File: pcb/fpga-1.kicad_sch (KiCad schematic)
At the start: 2 parts

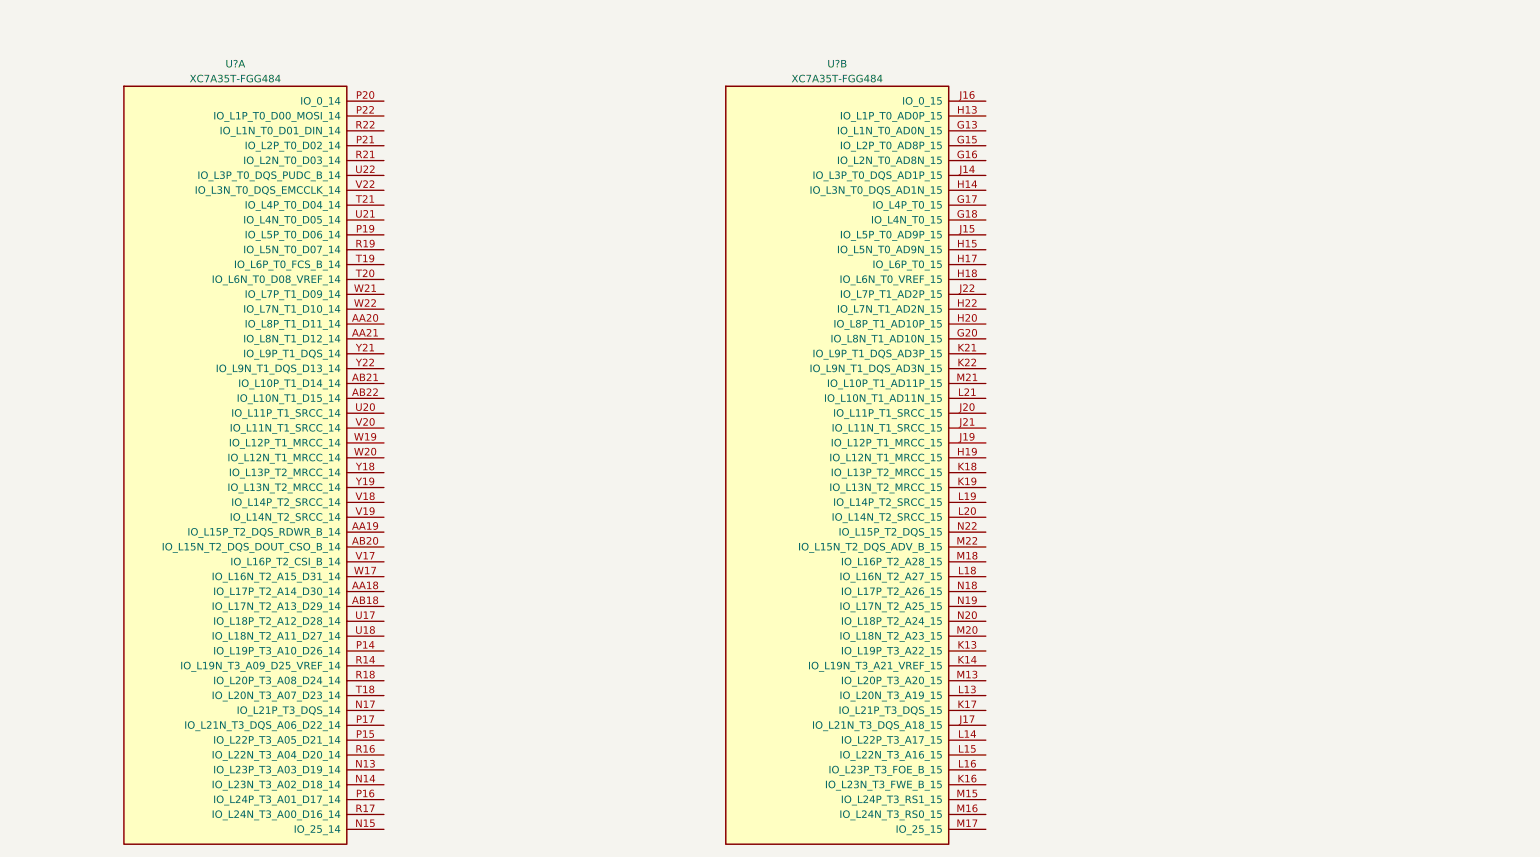
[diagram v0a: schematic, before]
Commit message: add sensors, hierarchical changes
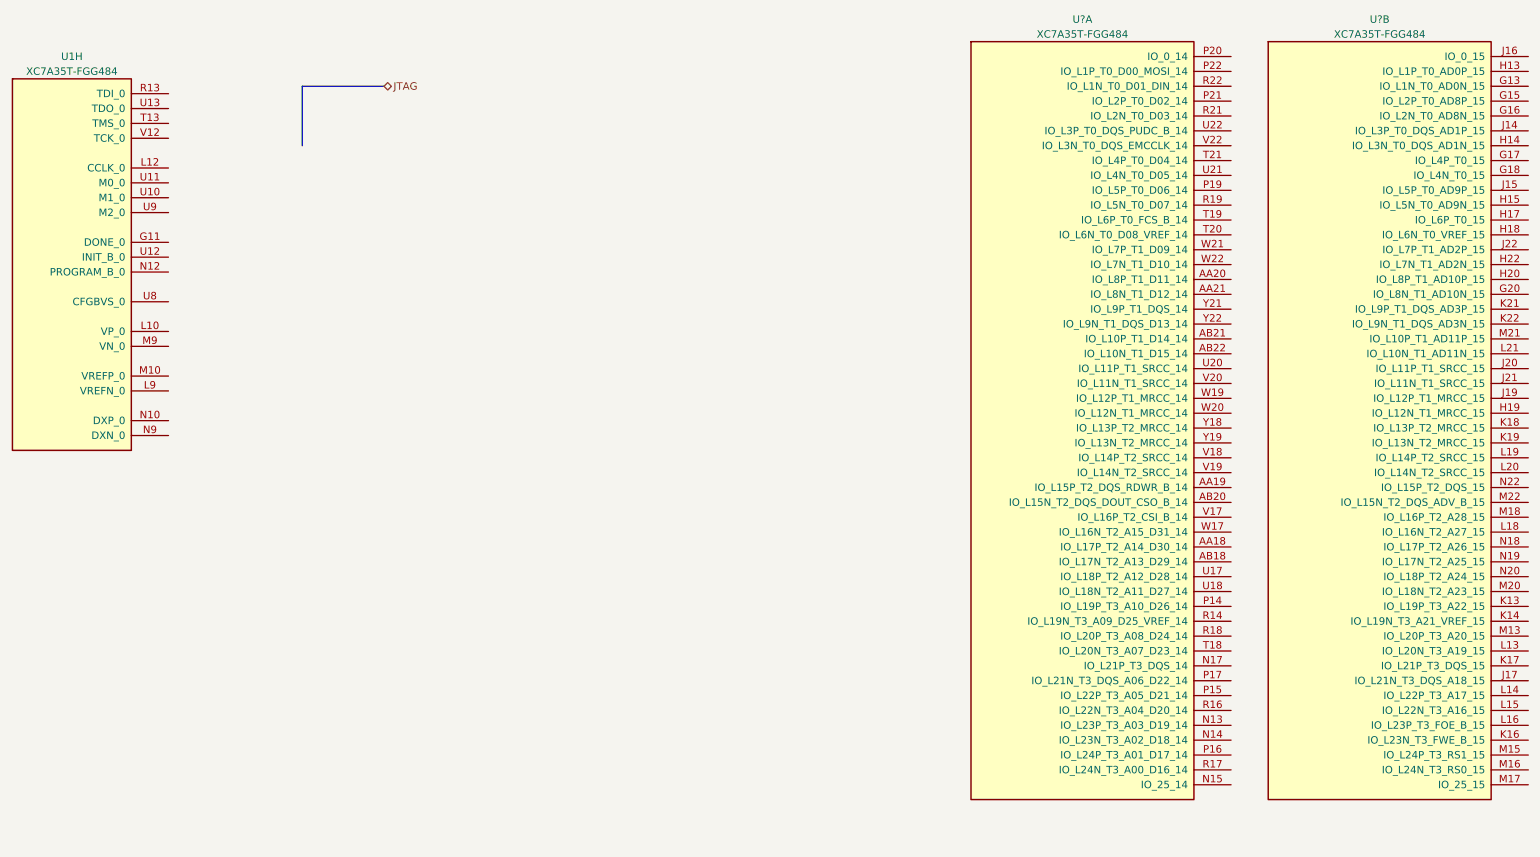
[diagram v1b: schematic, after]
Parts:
- added U1: XC7A35T-FGG484, Package_BGA:Xilinx_FGG484, symbol FPGA_Xilinx_Artix7:XC7A35T-FGG484
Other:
- moved on the sheet: U?A, U?B

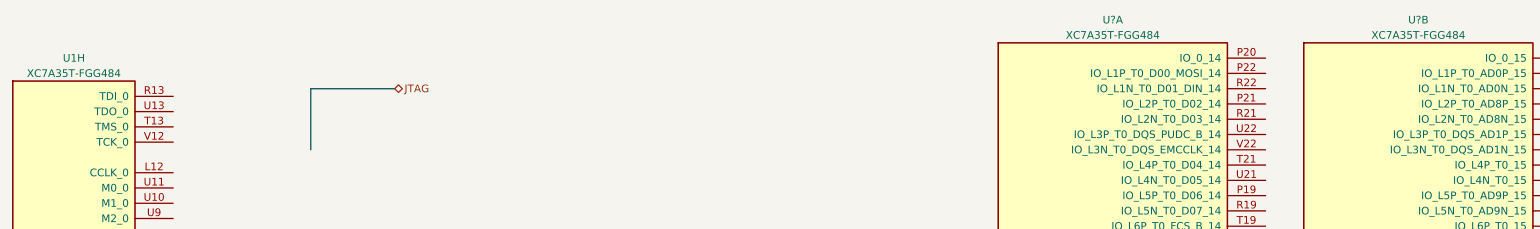
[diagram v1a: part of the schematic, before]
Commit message: addl. updates to power hierarchy
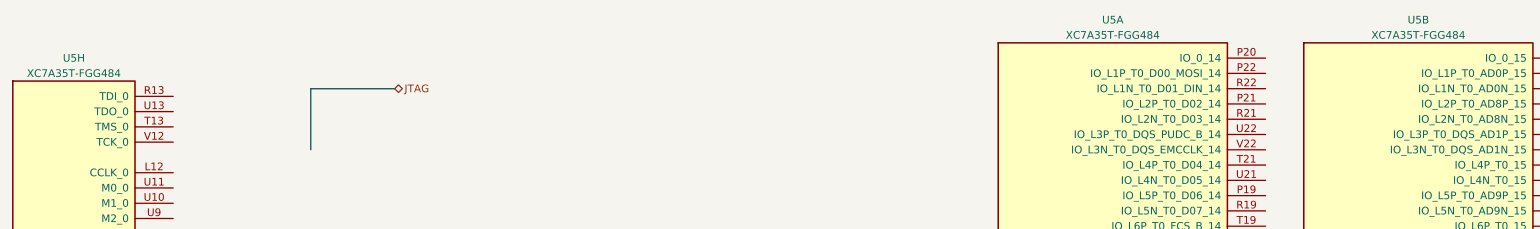
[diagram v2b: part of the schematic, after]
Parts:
- gave numbers to parts that had none: 1
- renumbered U1 to U5
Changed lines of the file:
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@@
 		(dnp no)
 		(fields_autoplaced yes)
-		(property "Reference" "U?"
+		(property "Reference" "U5"
 			(at 255.27 17.78 0)
 			(effects
@@
 			(project "RPi-HwAB-1"
 				(path "/e63e39d7-6ac0-4ffd-8aa3-1841a4541b55/74df7e7f-18cd-4565-8339-2ea0b43d6ca3"
-					(reference "U?")
+					(reference "U5")
 					(unit 2)
 				)
@@
 		(dnp no)
 		(fields_autoplaced yes)
-		(property "Reference" "U?"
+		(property "Reference" "U5"
 			(at 204.47 17.78 0)
 			(effects
@@
 			(project "RPi-HwAB-1"
 				(path "/e63e39d7-6ac0-4ffd-8aa3-1841a4541b55/74df7e7f-18cd-4565-8339-2ea0b43d6ca3"
-					(reference "U?")
+					(reference "U5")
 					(unit 1)
 				)
@@
 		(dnp no)
 		(fields_autoplaced yes)
-		(property "Reference" "U1"
+		(property "Reference" "U5"
 			(at 31.75 24.13 0)
 			(effects
@@
 			(project "RPi-HwAB-1"
 				(path "/e63e39d7-6ac0-4ffd-8aa3-1841a4541b55/74df7e7f-18cd-4565-8339-2ea0b43d6ca3"
-					(reference "U1")
+					(reference "U5")
 					(unit 8)
 				)

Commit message: added power sequencing through raspi gpio
additionally defined sensors
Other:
- company: (none) -> Andre S Winkel
- title: (none) -> RPi HwAB HAT+
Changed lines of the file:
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@@
 	(generator_version "9.0")
 	(paper "A4")
+	(title_block
+		(title "RPi HwAB HAT+")
+		(date "2025-08-23")
+		(rev "01")
+		(company "Andre S Winkel")
+	)
 	(bus
 		(pts

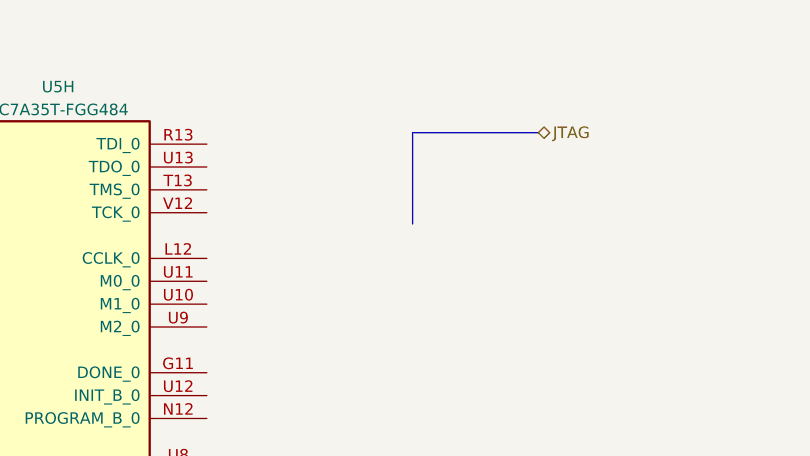
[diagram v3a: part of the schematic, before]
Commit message: added power supply simulations
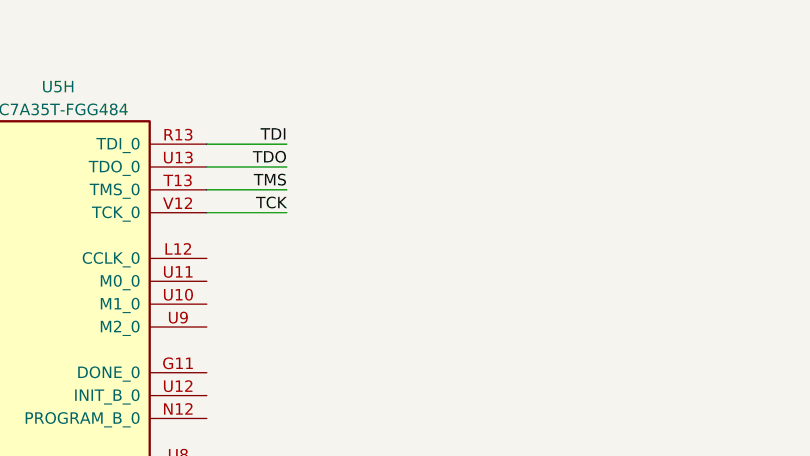
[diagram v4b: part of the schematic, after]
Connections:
- net TDI: now reaches U5.R13 (TDI_0)
- net TMS: now reaches U5.T13 (TMS_0)
- net TDO: now reaches U5.U13 (TDO_0)
- net TCK: now reaches U5.V12 (TCK_0)
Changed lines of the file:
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@@
 		(company "Andre S Winkel")
 	)
-	(bus
+	(wire
 		(pts
-			(xy 71.12 29.21) (xy 71.12 39.37)
+			(xy 48.26 30.48) (xy 57.15 30.48)
 		)
 		(stroke
@@
 		)
 	)
-	(bus
+	(wire
 		(pts
-			(xy 85.09 29.21) (xy 71.12 29.21)
+			(xy 48.26 33.02) (xy 57.15 33.02)
 		)
 		(stroke
@@
 		)
 	)
-	(hierarchical_label "JTAG"
-		(shape bidirectional)
-		(at 85.09 29.21 0)
+	(wire
+		(pts
+			(xy 48.26 35.56) (xy 57.15 35.56)
+		)
+		(stroke
+			(width 0)
+			(type default)
+		)
+	)
+	(wire
+		(pts
+			(xy 48.26 38.1) (xy 57.15 38.1)
+		)
+		(stroke
+			(width 0)
+			(type default)
+		)
+	)
+	(label "TDO"
+		(at 57.15 33.02 180)
 		(effects
 			(font
 				(size 1.27 1.27)
 			)
-			(justify left)
+			(justify right bottom)
 		)
 	)
+	(label "TCK"
+		(at 57.15 38.1 180)
+		(effects
+			(font
+				(size 1.27 1.27)
+			)
+			(justify right bottom)
+		)
+	)
+	(label "TMS"
+		(at 57.15 35.56 180)
+		(effects
+			(font
+				(size 1.27 1.27)
+			)
+			(justify right bottom)
+		)
+	)
+	(label "TDI"
+		(at 57.15 30.48 180)
+		(effects
+			(font
+				(size 1.27 1.27)
+			)
+			(justify right bottom)
+		)
+	)

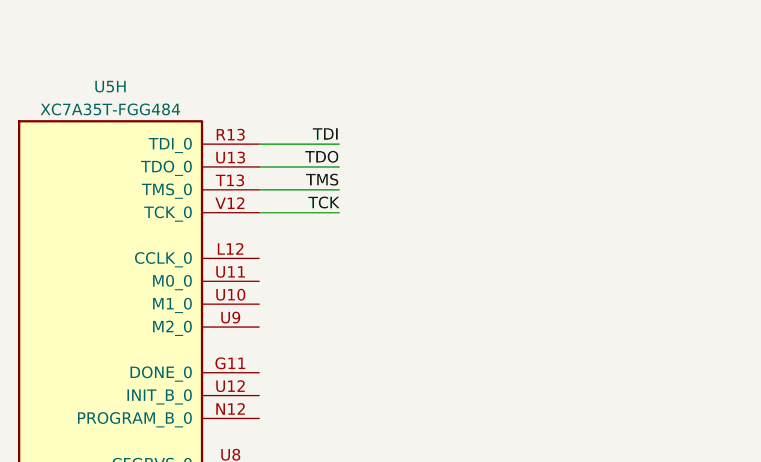
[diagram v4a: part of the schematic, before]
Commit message: connected jtag-fpga, tc2030
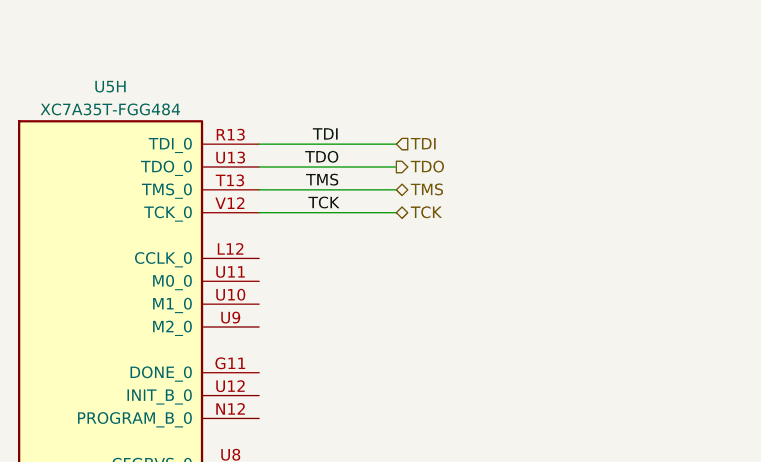
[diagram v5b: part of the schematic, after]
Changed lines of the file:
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@@
 	(wire
 		(pts
-			(xy 48.26 30.48) (xy 57.15 30.48)
+			(xy 48.26 30.48) (xy 63.5 30.48)
 		)
 		(stroke
@@
 	(wire
 		(pts
-			(xy 48.26 33.02) (xy 57.15 33.02)
+			(xy 48.26 33.02) (xy 63.5 33.02)
 		)
 		(stroke
@@
 	(wire
 		(pts
-			(xy 48.26 35.56) (xy 57.15 35.56)
+			(xy 48.26 35.56) (xy 63.5 35.56)
 		)
 		(stroke
@@
 	(wire
 		(pts
-			(xy 48.26 38.1) (xy 57.15 38.1)
+			(xy 48.26 38.1) (xy 63.5 38.1)
 		)
 		(stroke
@@
 		)
 	)
+	(hierarchical_label "TDI"
+		(shape input)
+		(at 63.5 30.48 0)
+		(effects
+			(font
+				(size 1.27 1.27)
+			)
+			(justify left)
+		)
+	)
+	(hierarchical_label "TDO"
+		(shape output)
+		(at 63.5 33.02 0)
+		(effects
+			(font
+				(size 1.27 1.27)
+			)
+			(justify left)
+		)
+	)
+	(hierarchical_label "TCK"
+		(shape bidirectional)
+		(at 63.5 38.1 0)
+		(effects
+			(font
+				(size 1.27 1.27)
+			)
+			(justify left)
+		)
+	)
+	(hierarchical_label "TMS"
+		(shape bidirectional)
+		(at 63.5 35.56 0)
+		(effects
+			(font
+				(size 1.27 1.27)
+			)
+			(justify left)
+		)
+	)

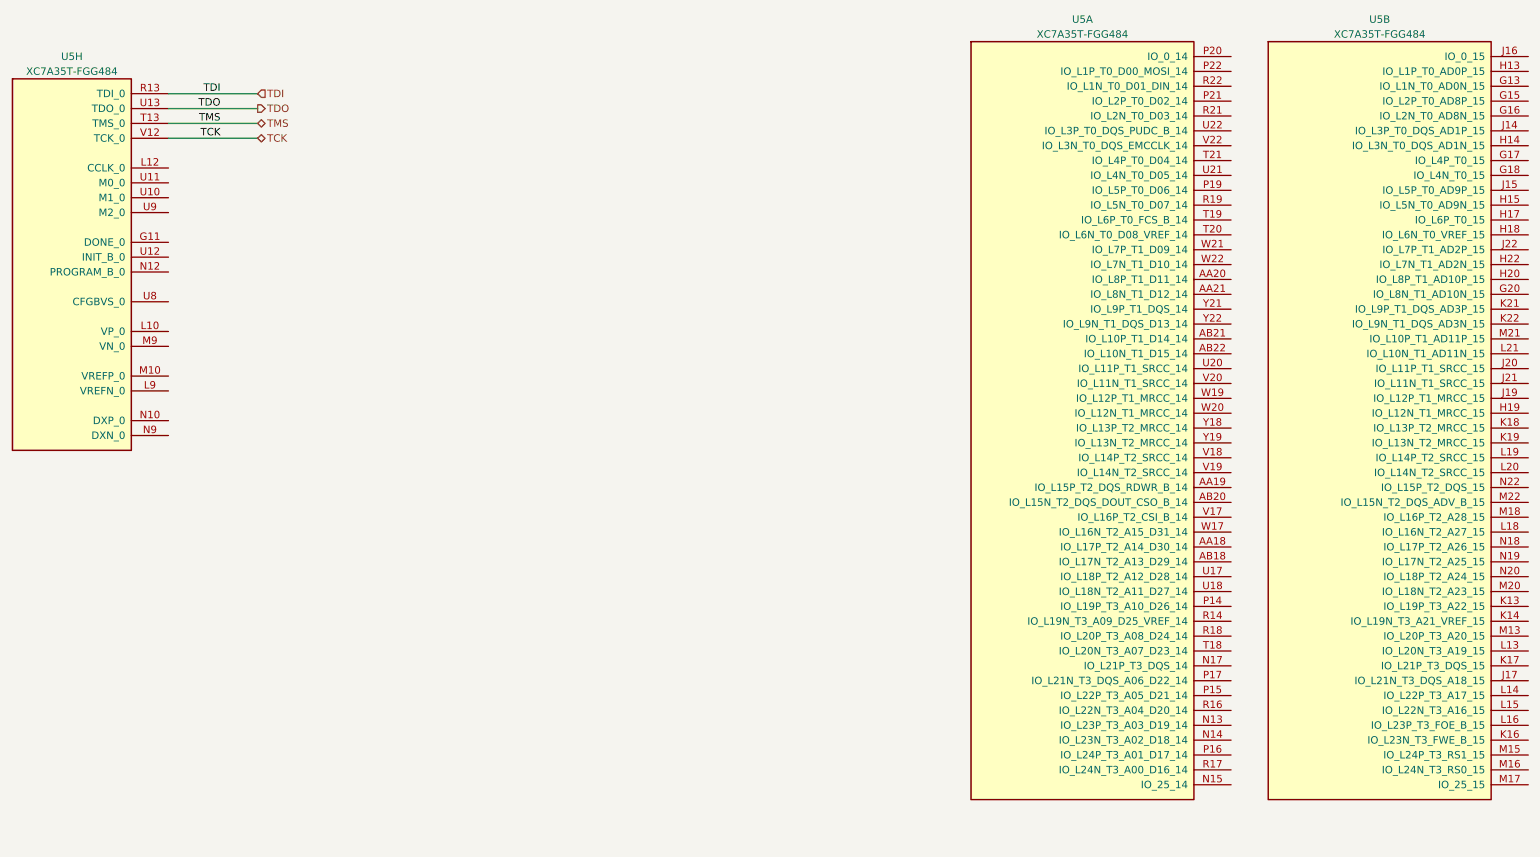
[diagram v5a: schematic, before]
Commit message: reorg hierarchical, define buses
added bus definitions, aliasing, reorganized sub-sheets for hierarchical interpretation, grouped fpga. pending dram and mram addition
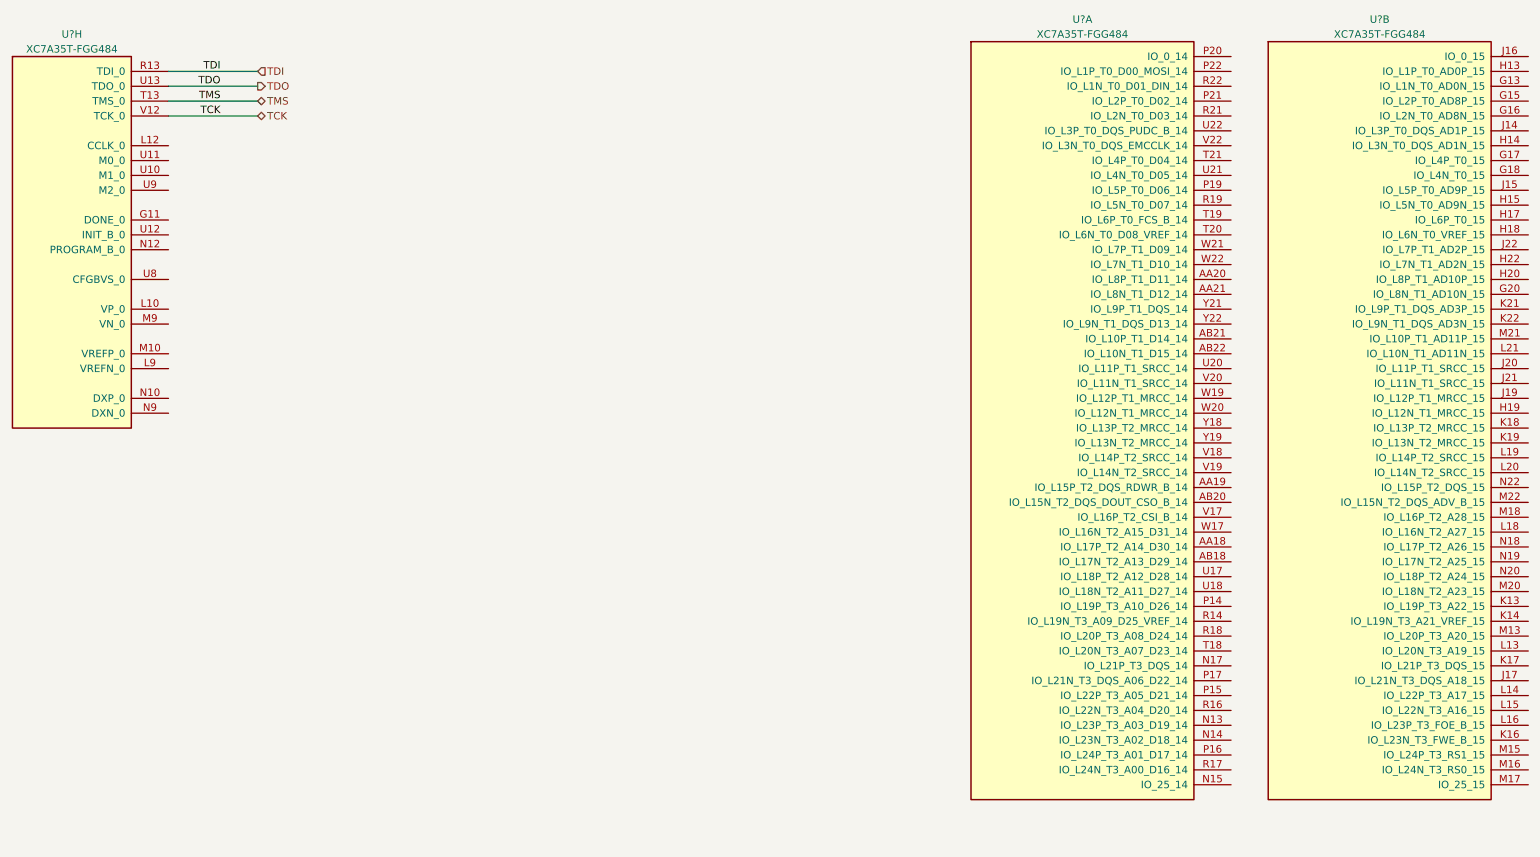
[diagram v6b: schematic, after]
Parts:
- renumbered U5 to U?
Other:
- moved on the sheet: U?H
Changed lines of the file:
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@@
 	(wire
 		(pts
-			(xy 48.26 30.48) (xy 63.5 30.48)
+			(xy 48.26 26.67) (xy 63.5 26.67)
 		)
 		(stroke
@@
 	(wire
 		(pts
-			(xy 48.26 33.02) (xy 63.5 33.02)
+			(xy 48.26 29.21) (xy 63.5 29.21)
 		)
 		(stroke
@@
 	(wire
 		(pts
-			(xy 48.26 35.56) (xy 63.5 35.56)
+			(xy 48.26 31.75) (xy 63.5 31.75)
 		)
 		(stroke
@@
 	(wire
 		(pts
-			(xy 48.26 38.1) (xy 63.5 38.1)
+			(xy 48.26 34.29) (xy 63.5 34.29)
 		)
 		(stroke
@@
 	)
 	(label "TDO"
-		(at 57.15 33.02 180)
+		(at 57.15 29.21 180)
 		(effects
 			(font
@@
 	)
 	(label "TCK"
-		(at 57.15 38.1 180)
+		(at 57.15 34.29 180)
 		(effects
 			(font
@@
 	)
 	(label "TMS"
-		(at 57.15 35.56 180)
+		(at 57.15 31.75 180)
 		(effects
 			(font
@@
 	)
 	(label "TDI"
-		(at 57.15 30.48 180)
+		(at 57.15 26.67 180)
 		(effects
 			(font
@@
 	(hierarchical_label "TDI"
 		(shape input)
-		(at 63.5 30.48 0)
+		(at 63.5 26.67 0)
 		(effects
 			(font
@@
 	(hierarchical_label "TDO"
 		(shape output)
-		(at 63.5 33.02 0)
+		(at 63.5 29.21 0)
 		(effects
 			(font
@@
 	(hierarchical_label "TCK"
 		(shape bidirectional)
-		(at 63.5 38.1 0)
+		(at 63.5 34.29 0)
 		(effects
 			(font
@@
 	(hierarchical_label "TMS"
 		(shape bidirectional)
-		(at 63.5 35.56 0)
+		(at 63.5 31.75 0)
 		(effects
 			(font
@@
 		(dnp no)
 		(fields_autoplaced yes)
-		(property "Reference" "U5"
+		(property "Reference" "U?"
 			(at 255.27 17.78 0)
 			(effects
@@
 		(instances
 			(project "RPi-HwAB-1"
-				(path "/e63e39d7-6ac0-4ffd-8aa3-1841a4541b55/74df7e7f-18cd-4565-8339-2ea0b43d6ca3"
-					(reference "U5")
+				(path "/e63e39d7-6ac0-4ffd-8aa3-1841a4541b55/59d21473-a004-4514-8090-fd93db818925/350bfe7d-9948-4ca7-a542-a75eb385def4"
+					(reference "U?")
 					(unit 2)
 				)
@@
 		(dnp no)
 		(fields_autoplaced yes)
-		(property "Reference" "U5"
+		(property "Reference" "U?"
 			(at 204.47 17.78 0)
 			(effects
@@
 		(instances
 			(project "RPi-HwAB-1"
-				(path "/e63e39d7-6ac0-4ffd-8aa3-1841a4541b55/74df7e7f-18cd-4565-8339-2ea0b43d6ca3"
-					(reference "U5")
+				(path "/e63e39d7-6ac0-4ffd-8aa3-1841a4541b55/59d21473-a004-4514-8090-fd93db818925/350bfe7d-9948-4ca7-a542-a75eb385def4"
+					(reference "U?")
 					(unit 1)
 				)
@@
 	(symbol
 		(lib_id "FPGA_Xilinx_Artix7:XC7A35T-FGG484")
-		(at 31.75 59.69 0)
+		(at 31.75 55.88 0)
 		(unit 8)
 		(exclude_from_sim no)
@@
 		(dnp no)
 		(fields_autoplaced yes)
-		(property "Reference" "U5"
-			(at 31.75 24.13 0)
+		(property "Reference" "U?"
+			(at 31.75 20.32 0)
 			(effects
 				(font
@@
 		)
 		(property "Value" "XC7A35T-FGG484"
-			(at 31.75 26.67 0)
+			(at 31.75 22.86 0)
 			(effects
 				(font
@@
 		)
 		(property "Footprint" "Package_BGA:Xilinx_FGG484"
-			(at 31.75 59.69 0)
+			(at 31.75 55.88 0)
 			(effects
 				(font
@@
 		)
 		(property "Datasheet" ""
-			(at 31.75 59.69 0)
+			(at 31.75 55.88 0)
 			(effects
 				(font
@@
 		)
 		(property "Description" "Artix 7 T 35 XC7A35T-FGG484"
-			(at 5.08 43.18 0)
+			(at 5.08 39.37 0)
 			(effects
 				(font
@@
 		(instances
 			(project "RPi-HwAB-1"
-				(path "/e63e39d7-6ac0-4ffd-8aa3-1841a4541b55/74df7e7f-18cd-4565-8339-2ea0b43d6ca3"
-					(reference "U5")
+				(path "/e63e39d7-6ac0-4ffd-8aa3-1841a4541b55/59d21473-a004-4514-8090-fd93db818925/350bfe7d-9948-4ca7-a542-a75eb385def4"
+					(reference "U?")
 					(unit 8)
 				)
